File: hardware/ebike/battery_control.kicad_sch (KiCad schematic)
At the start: 0 parts

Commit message: first draft of motor control circuitry, need to annotate still
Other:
- note added: "Implement current sensing + voltage divider to determine battery percentage"
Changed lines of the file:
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@@
 	(generator_version "9.0")
 	(paper "A4")
+	(text "Implement current sensing + voltage divider to determine battery percentage"
+		(exclude_from_sim no)
+		(at 134.112 38.862 0)
+		(effects
+			(font
+				(size 1.27 1.27)
+			)
+		)
+	)
 )

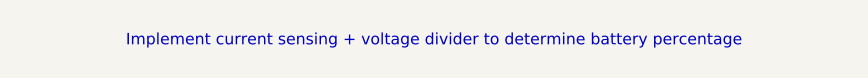
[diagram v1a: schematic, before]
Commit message: Wired PWM, ADC to MCU. Added HAL filtration + battery decoupling
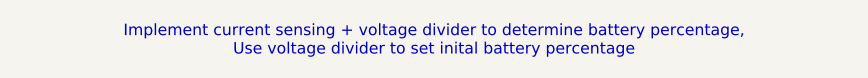
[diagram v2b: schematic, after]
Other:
- note added: "Implement current sensing + voltage divider to determine battery percentage, Use voltage divider to set inital battery percentage"
- note removed: "Implement current sensing + voltage divider to determine battery percentage"
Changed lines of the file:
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@@
 	(generator_version "9.0")
 	(paper "A4")
-	(text "Implement current sensing + voltage divider to determine battery percentage"
+	(text "Implement current sensing + voltage divider to determine battery percentage,\nUse voltage divider to set inital battery percentage"
 		(exclude_from_sim no)
 		(at 134.112 38.862 0)
